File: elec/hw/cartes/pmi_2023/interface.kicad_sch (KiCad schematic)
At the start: 31 parts, among them SW3 MSS12C02LS-BB2.0, SW5 DS1040-04RN, SW6 2425755-1, U11 XRA1200PIG16TR-F, U18 EESX1321

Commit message: wip
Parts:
- R80, R81: now not fitted
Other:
- note added: "starting cord"
- moved on the sheet: C31

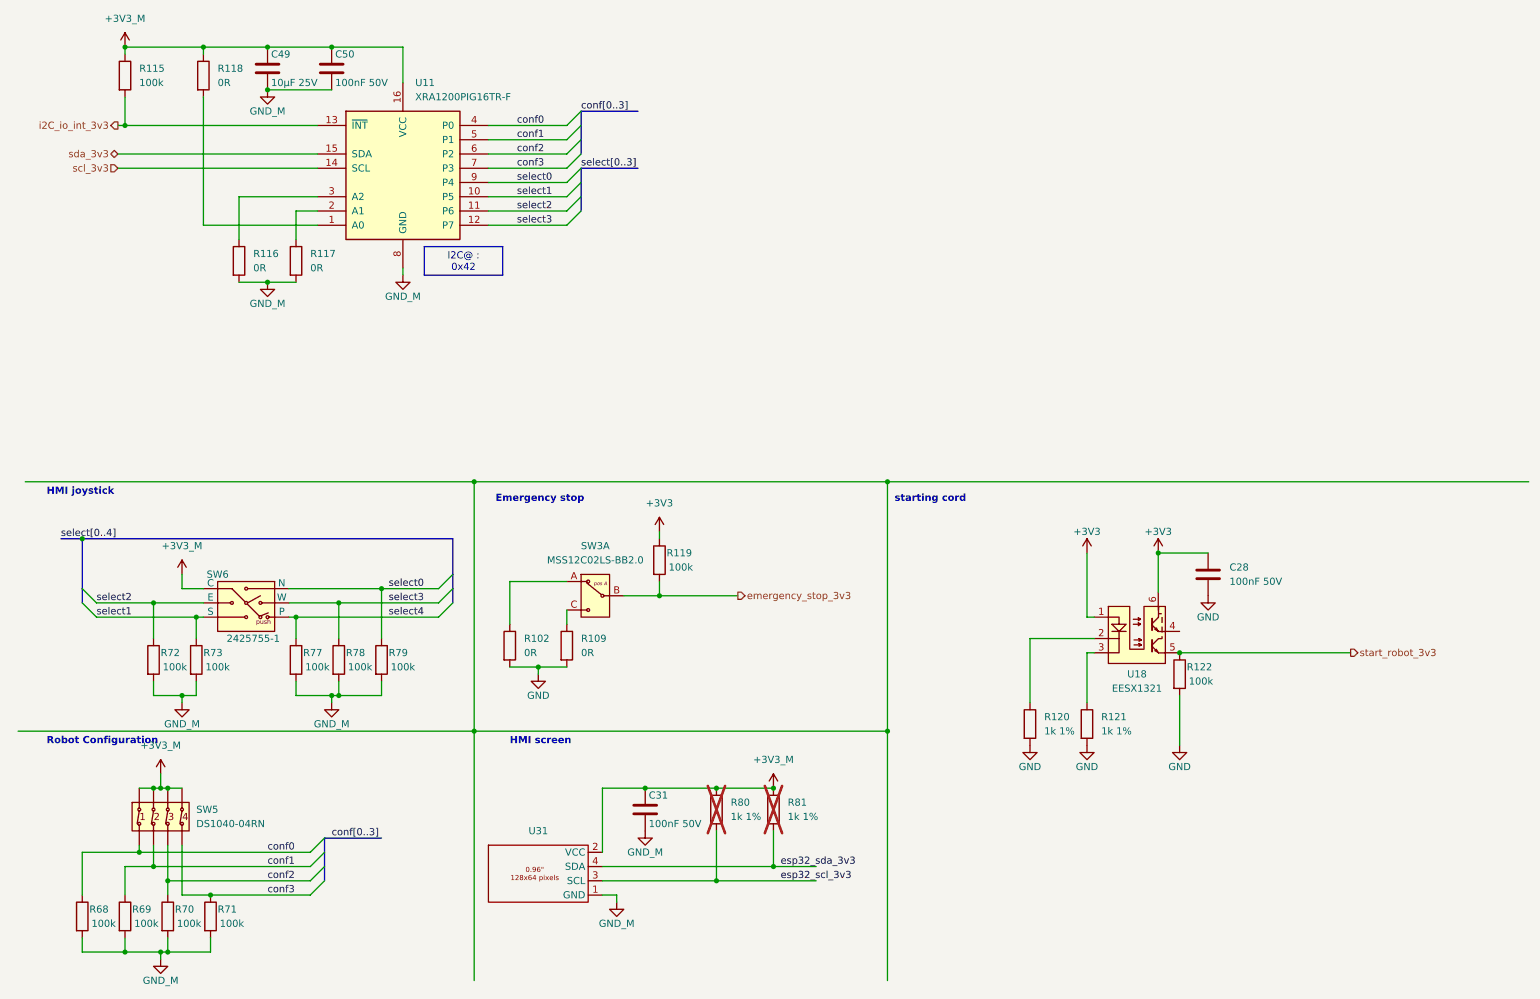
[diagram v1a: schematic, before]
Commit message: front and back tof added, selector changed, ready to route
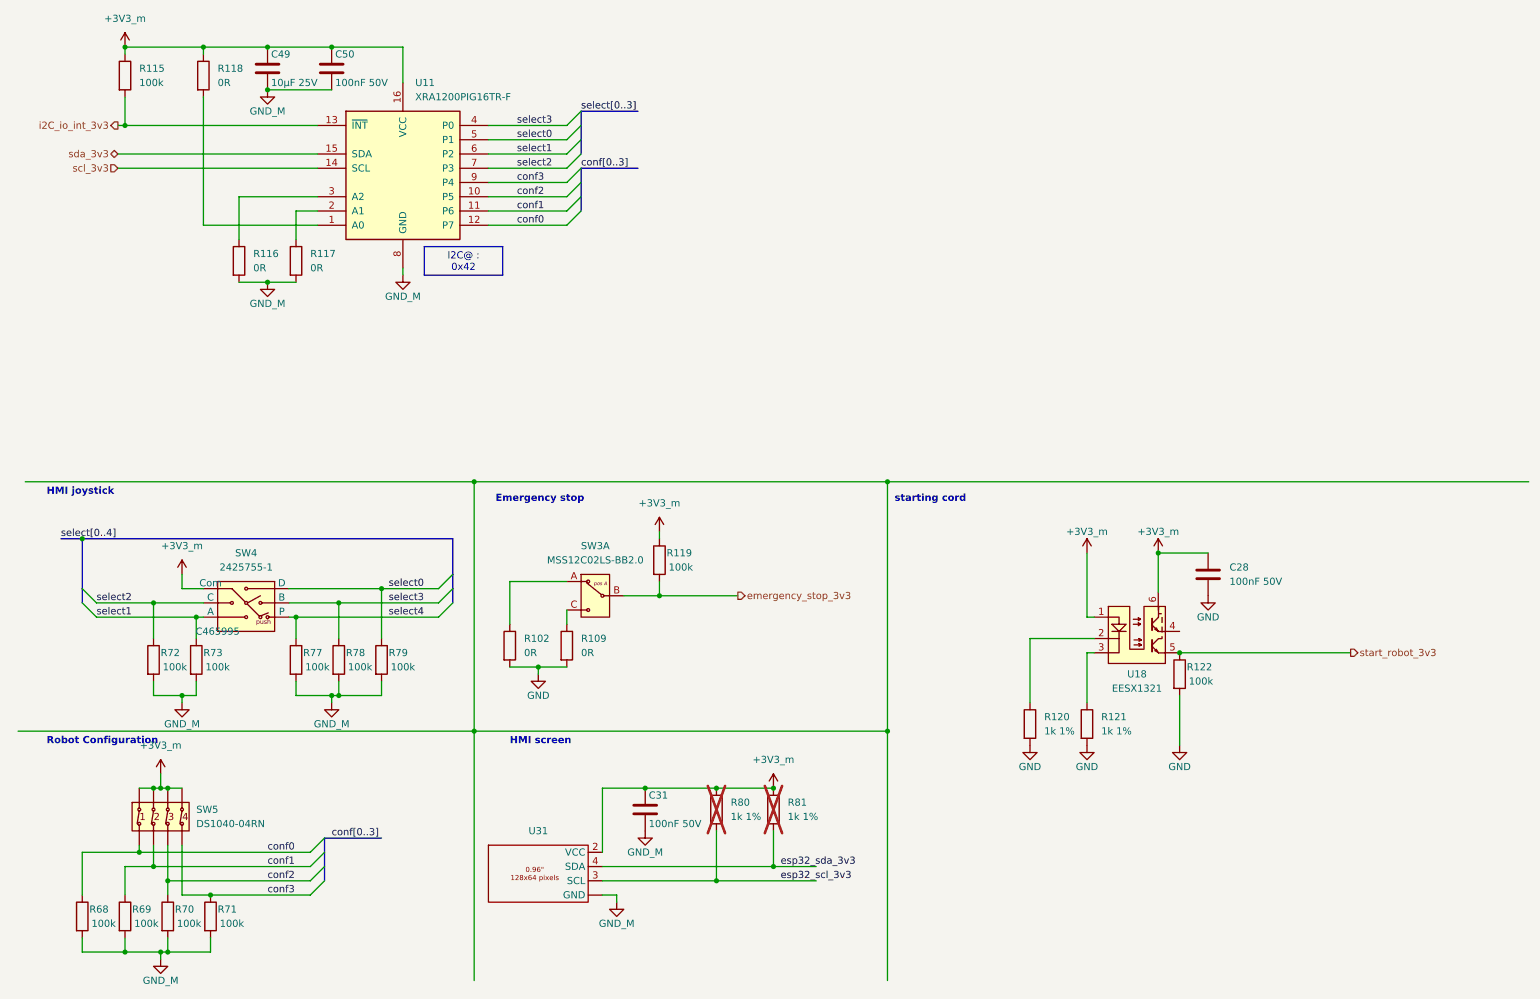
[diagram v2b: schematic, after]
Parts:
- removed SW6: 2425755-1, cocotter_connectors:2425755-1, symbol cocotter_connectors:2425755-1
- added SW4: 2425755-1, cocotter_connectors:TM-4175-B-A, symbol cocotter_connectors:TM-4175-B-A
- R102, R109, R116, R117, R118: JLCPCB C21189 -> C431718
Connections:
- net +3V3 is gone; now on net +3V3_m: C28.1, R119.1, U18.1 (A), U18.6 (C)
- net +3V3_m: now also SW4.5 (Com)
- net GND_M: now also U31. (GND); no longer U31.1 (GND)
- net conf0: now also U11.12 (P7); no longer U11.4 (P0)
- net conf1: now also U11.11 (P6); no longer U11.5 (P1)
- net conf2: now also U11.10 (P5); no longer U11.6 (P2)
- net conf3: now also U11.9 (P4); no longer U11.7 (P3)
- net select0: now also U11.5 (P1), SW4.6 (D); no longer U11.9 (P4)
- net select1: now also U11.6 (P2), SW4.1 (A); no longer U11.10 (P5)
- net select2: now also U11.7 (P3), SW4.3 (C); no longer U11.11 (P6)
- net select3: now also U11.4 (P0), SW4.4 (B); no longer U11.12 (P7)
- net select4: now also SW4.2 (P)

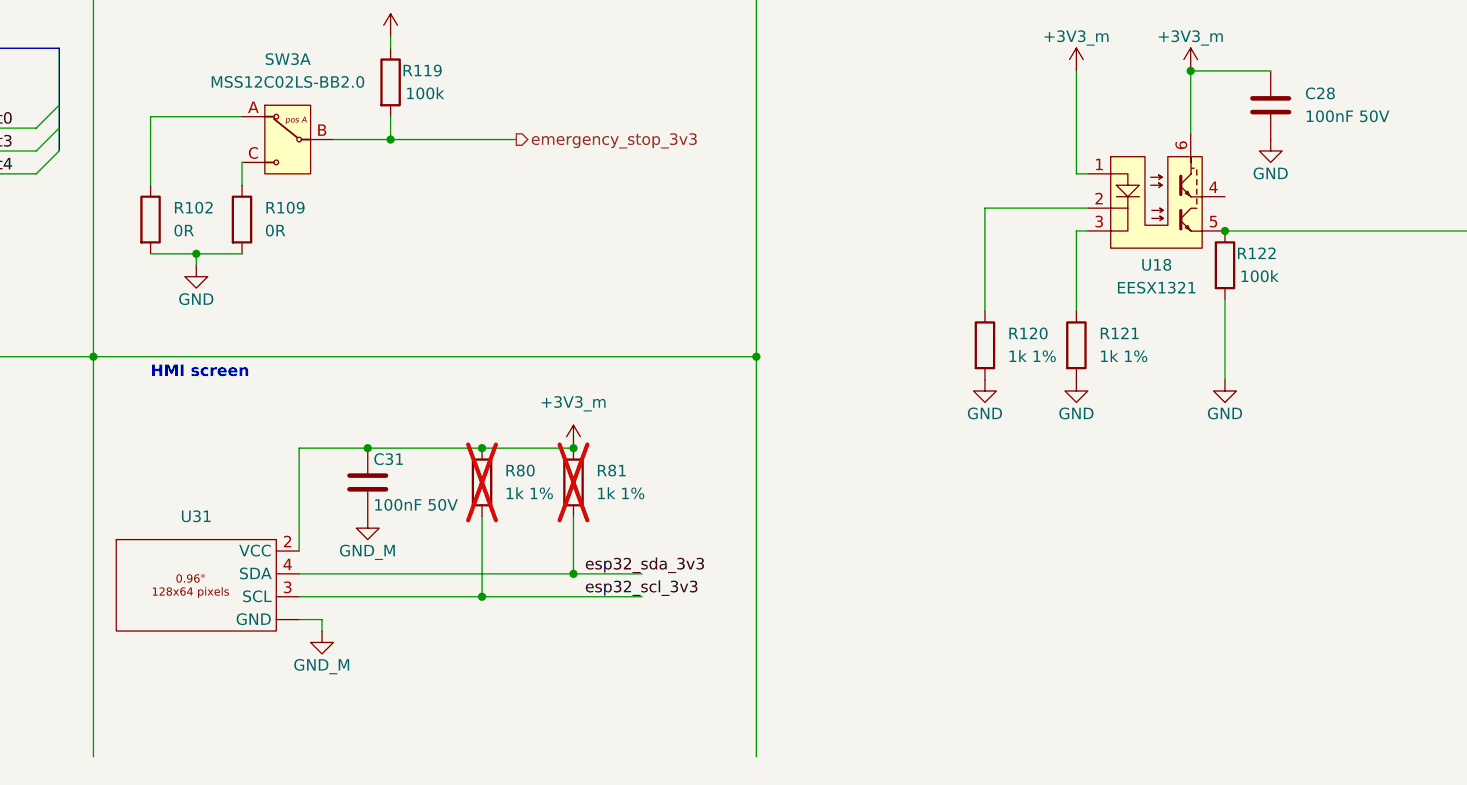
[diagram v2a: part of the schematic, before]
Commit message: corrected librariesand ongoing routing
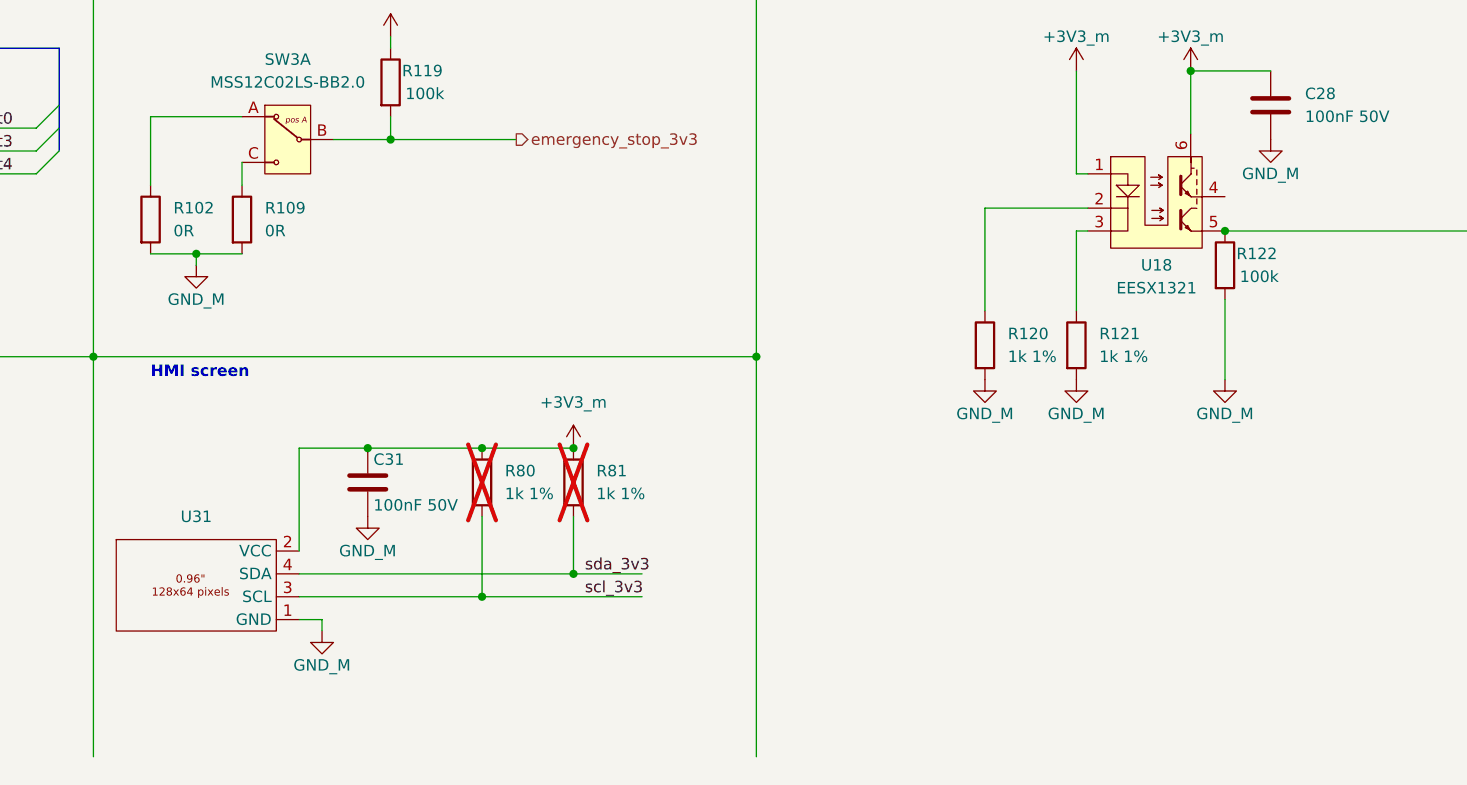
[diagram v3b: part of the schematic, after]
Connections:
- net GND is gone; now on net GND_M: C28.2, R102.2, R109.2, R120.2, R121.2, R122.2
- net esp32_scl_3v3 is gone; now on net scl_3v3: R80.2, U31.3 (SCL)
- net esp32_sda_3v3 is gone; now on net sda_3v3: R81.2, U31.4 (SDA)
- net GND_M: now also U31.1 (GND); no longer U31. (GND)
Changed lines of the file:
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@@
 		)
 	)
-	(label "esp32_sda_3v3"
+	(label "sda_3v3"
 		(at 149.86 175.26 0)
 		(fields_autoplaced yes)
@@
 		)
 	)
-	(label "esp32_scl_3v3"
+	(label "scl_3v3"
 		(at 149.86 177.8 0)
 		(fields_autoplaced yes)
@@
 			)
 		)
-		(property "Value" "GND"
+		(property "Value" "GND_M"
 			(at 106.68 144.78 0)
 			(effects
@@
 			)
 		)
-		(property "Description" ""
+		(property "Description" "0.96 inches, 128x64 pixels, supply [3.3;5V], I2C, SH1106 (or SSD1306) controller"
 			(at 106.68 176.53 0)
 			(effects
@@
 			)
 		)
-		(pin ""
+		(pin "1"
 		)
 		(pin "2"
@@
 			)
 		)
-		(property "Value" "GND"
+		(property "Value" "GND_M"
 			(at 220.98 157.48 0)
 			(effects
@@
 			)
 		)
-		(property "Value" "GND"
+		(property "Value" "GND_M"
 			(at 194.31 157.48 0)
 			(effects
@@
 			)
 		)
-		(property "Value" "GND"
+		(property "Value" "GND_M"
 			(at 226.06 130.81 0)
 			(effects
@@
 			)
 		)
-		(property "Value" "GND"
+		(property "Value" "GND_M"
 			(at 204.47 157.48 0)
 			(effects

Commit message: wip
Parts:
- R120, R121, R80, R81: Specification 1k 0603 1% 100mW -> 10k 0603 1% 100mW; mouser (none) -> 603-RC0603FR-10100KL
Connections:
- net conf3: no longer U11.9 (P4)
- net select2: now also U11.9 (P4); no longer U11.7 (P3)
- net select4: now also U11.7 (P3)

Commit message: added oled display power supply res selectors, jlcpcb refs : wip
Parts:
- added R132, R133, R134, R135: 0R, cocotter_resistor:r0603_reflow, symbol cocotter_resistors:R_0R_0603
- C49: symbol cocotter_capacitors:C_10µF_16V_0805_X5R -> cocotter_capacitors:C_10µF_25V_0805_X5R; Specification 10µF 25V X5R 0805 -> 10µF 25V X7R 0805
- U31: now left out of the parts list
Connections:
- net start_robot_3v3: no longer U18.5 (E2)
- net at R121.1: no longer U18.3 (C2)
- net at R120.1: now also U18.3 (C2); no longer U18.2 (C1)
- net +3V3_m renamed +3V3
- net +3V3: now also R132.2, R133.2; no longer C31.1, U18.1 (A), U18.6 (C), U31.2 (VCC)
- net GND_M renamed GND
- net GND: now also R134.2, R135.2; no longer U31.1 (GND)
- new net: C31.1, R132.1, R135.1, U31.2 (VCC)
- new net: R133.1, R134.1, U31.1 (GND)
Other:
- moved on the sheet: C31, R80, R81, U18

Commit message: reset button added to esp32 reset. uart prog connector replaces ftdi one
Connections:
- net +3V3 is gone; now on net +3V3_m: C28.1, C49.1, C50.1, R115.1, R118.1, R119.1, R132.2, R133.2, R80.1, R81.1, SW4.5 (Com), SW5.5, SW5.6, SW5.7, SW5.8, U11.16 (VCC)
- net start_robot_3v3: now also U18.5 (E2)
- net at R133.1, U31.1 (GND): now also R134.2; no longer R134.1
- net at R121.1: now also U18.3 (C2)
- net at R120.1: now also U18.2 (C1); no longer U18.3 (C2)
- net +3V3_m: now reaches U18.1 (A)
- net +3V3_m: now also U18.6 (C)
- net GND renamed GND_m
- net GND_m: now also R134.1; no longer R134.2
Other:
- moved on the sheet: R134, R135, U18

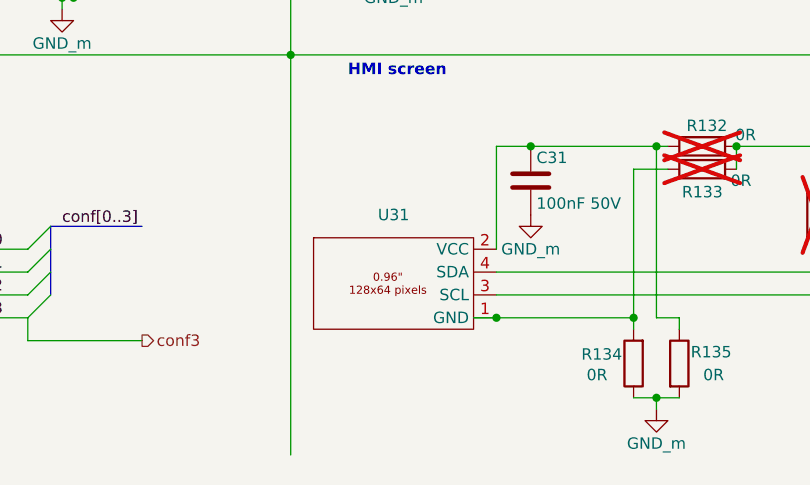
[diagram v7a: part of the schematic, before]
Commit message: PAMI 2023: update jlc part number
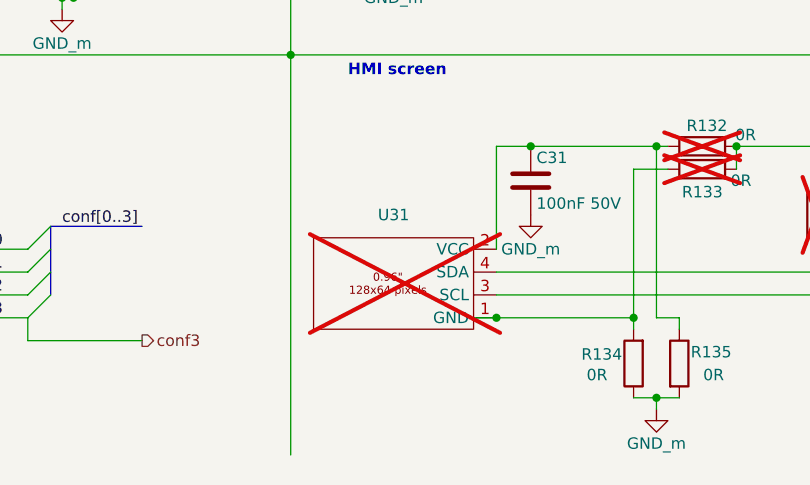
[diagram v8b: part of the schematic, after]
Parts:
- R120, R121: JLCPCB C2991540 -> C21190
- U11: JLCPCB (none) -> C2669711
- U31: now not fitted
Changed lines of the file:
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@@
 		(in_bom no)
 		(on_board yes)
-		(dnp no)
+		(dnp yes)
 		(fields_autoplaced yes)
 		(property "Reference" "U31"
@@
 			)
 		)
-		(property "JLCPCB" "C2991540"
+		(property "JLCPCB" "C21190"
 			(at 204.47 149.86 0)
 			(effects
@@
 			)
 		)
-		(property "JLCPCB" "C2991540"
+		(property "JLCPCB" "C21190"
 			(at 194.31 149.86 0)
 			(effects
@@
 			(effects
 				(font
+					(size 1.27 1.27)
+				)
+				(hide yes)
+			)
+		)
+		(property "JLCPCB" "C2669711"
+			(at 82.55 53.34 0)
+			(effects
+				(font
